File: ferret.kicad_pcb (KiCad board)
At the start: 2 copper layers, 122 parts, among them J201 Power, J301 BAT, J302 BAT, J303 SYS, J401 CHG, J402 CTRL, J403 SOICbite, J404 RS485, Q201 40V, Q202 40V, Q203 40V, SW201 Dead Battery, SW401 RESET, SW402 USER, U201 TPD6S300A, U202 FUSB307BMPX, U203 FSUSB42MUX, U301 TPS560430X3F, U302 BQ25792, U401 STM32F072CBTx, U402 CH340G, U403 SP3485EN, Y401 12MHz

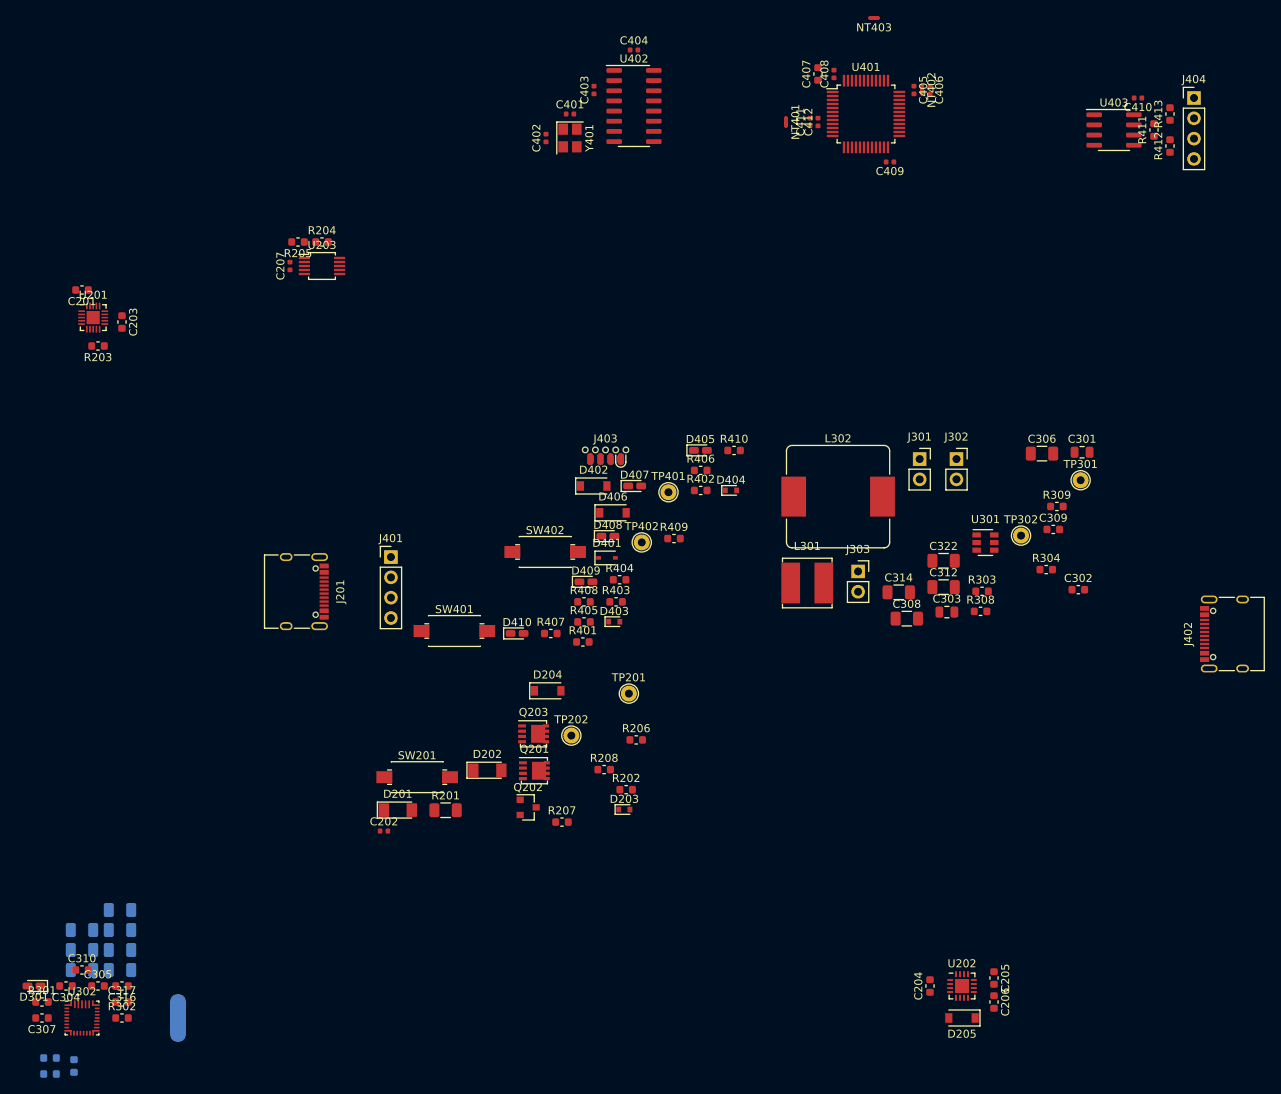
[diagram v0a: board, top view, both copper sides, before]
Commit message: placed to 50x50mm, started to route
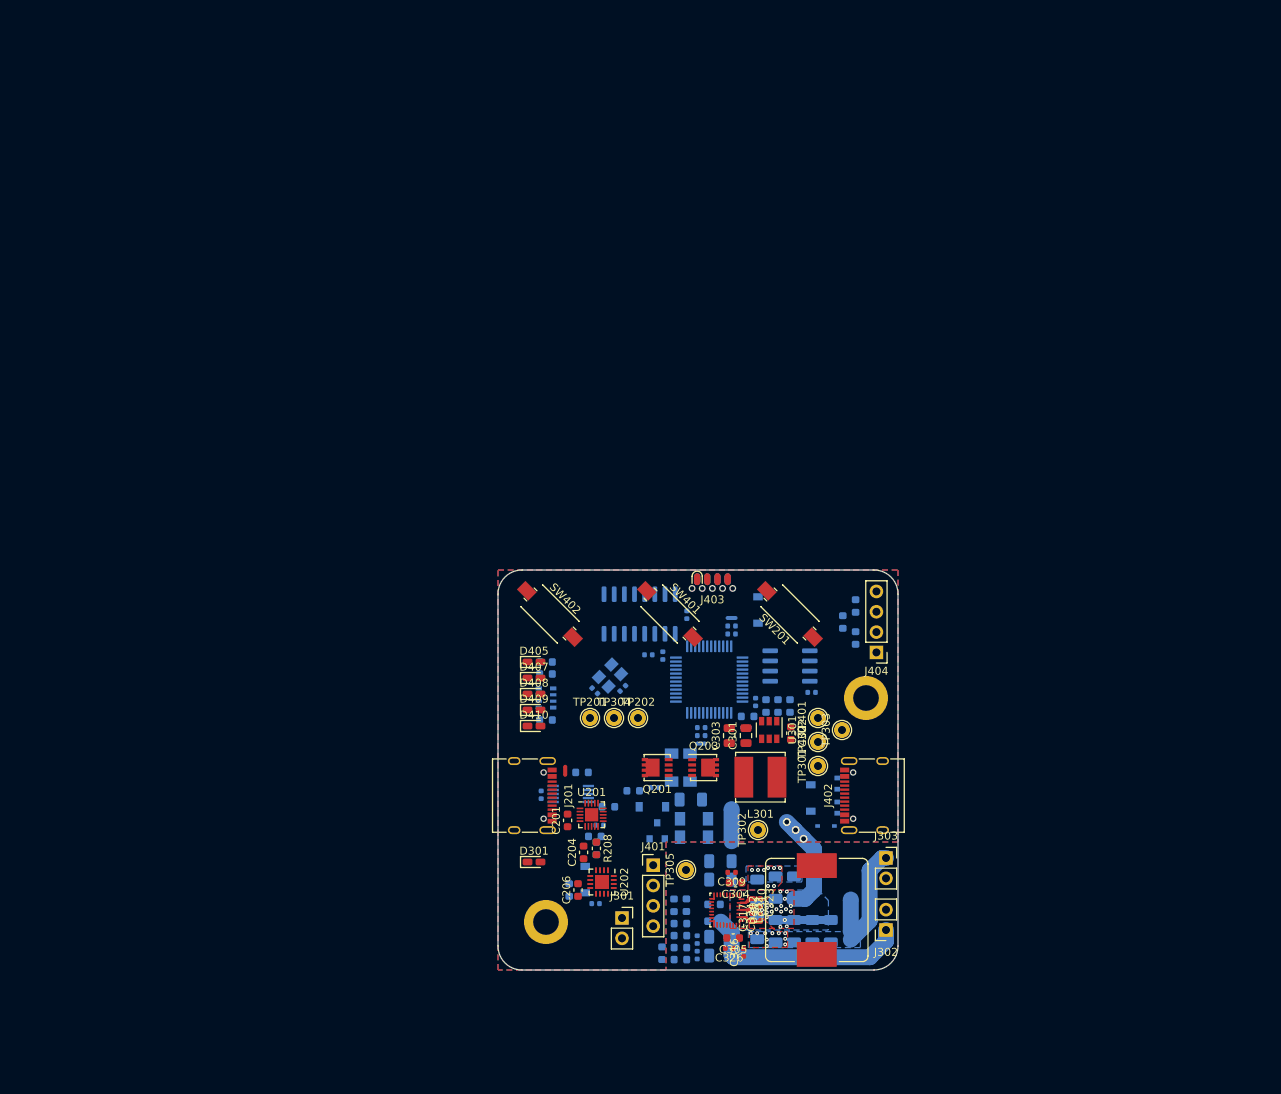
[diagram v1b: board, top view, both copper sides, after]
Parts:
- removed R407, R408, R409: 100, Resistor_SMD:R_0603_1608Metric
- added C323: 100nF, Capacitor_SMD:C_0402_1005Metric, F.Cu at (156.8, 129.6)
- added C324: 100nF, Capacitor_SMD:C_0402_1005Metric, F.Cu at (156.8, 131.4)
- added C326: 100nF, Capacitor_SMD:C_0402_1005Metric, F.Cu at (152.9, 135.3)
- added D206: 3V3, Diode_SMD:D_MiniMELF, B.Cu at (148.0, 112.7)
- added H101: MountingHole_Pad, MountingHole:MountingHole_3.2mm_M3_ISO14580_Pad, F.Cu at (170.0, 104.0)
- added H102: MountingHole_Pad, MountingHole:MountingHole_3.2mm_M3_ISO14580_Pad, F.Cu at (130.0, 132.0)
- added NT1: UwU, NetTie:NetTie-2_SMD_Pad0.5mm, F.Cu at (132.4, 113.1)
- added NT2: chonk_vbus, NetTie:NetTie-2_SMD_Pad2.0mm, B.Cu at (153.2, 119.9)
- added NT302: chonk, NetTie:NetTie-2_SMD_Pad2.0mm, B.Cu at (163.5, 126.0)
- added R310: 470, Resistor_SMD:R_0402_1005Metric, B.Cu at (148.9, 136.1)
- added TP303: GND, TestPoint:TestPoint_THTPad_D2.0mm_Drill1.0mm, F.Cu at (167.0, 108.0)
- added TP304: GND, TestPoint:TestPoint_THTPad_D2.0mm_Drill1.0mm, F.Cu at (138.5, 106.5)
- added TP305: GND1, TestPoint:TestPoint_THTPad_D2.0mm_Drill1.0mm, F.Cu at (147.5, 125.5)
- C202, C203, C205, C207, C306, C307, C308, C312, C314, C322, C401, C402, C403, C404, C405, C406, C407, C408, C409, C410, C411, C412, D201, D202, D204, D205, D401, D402, D403, D404, D406, NT401, NT402, NT403, Q202, R201, R202, R204, R205, R207, R301, R303, R304, R308, R309, R401, R402, R403, R404, R405, R410, R411, R412, R413, U203, U401, U402, U403, Y401: moved to B.Cu
- C309, C310, C316, C317: footprint Capacitor_SMD:C_0603_1608Metric -> Capacitor_SMD:C_0402_1005Metric
- D203: value 12V -> 5V6; footprint Diode_SMD:D_SOD-523 -> Diode_SMD:D_MiniMELF; moved to B.Cu
- R203, R206: footprint Resistor_SMD:R_0603_1608Metric -> Resistor_SMD:R_0402_1005Metric; moved to B.Cu
- R302: value 6.04k -> 5.6k; footprint Resistor_SMD:R_0603_1608Metric -> Resistor_SMD:R_0402_1005Metric; moved to B.Cu
- R406: value 100 -> 470; footprint Resistor_SMD:R_0603_1608Metric -> Resistor_SMD:R_Array_Convex_4x0603; moved to B.Cu
- TP302: value VBUS -> VBUS_BQ
- moved NT403 90.1 mm to (155.0, 107.7)
- moved C201 89.9 mm to (132.7, 119.3), turned to 90 degrees
- moved C311 89.2 mm to (161.0, 127.7), turned to 270 degrees
- moved U201 88.0 mm to (135.7, 118.6)
- moved C203 87.3 mm to (136.1, 121.3), turned to 0 degrees
- moved C313 87.1 mm to (158.7, 127.7), turned to 270 degrees
- moved R203 86.7 mm to (136.7, 119.9)
- moved C318 86.6 mm to (163.3, 133.2), turned to 90 degrees
- moved C307 85.2 mm to (151.0, 129.8)
- moved NT301 85.1 mm to (168.1, 131.2), turned to 270 degrees
- moved C315 85.0 mm to (156.4, 128.1), turned to 270 degrees
- moved C410 84.8 mm to (163.2, 103.3), turned to 0 degrees
- moved C304 84.7 mm to (153.7, 127.1)
- moved C319 84.3 mm to (161.0, 133.2), turned to 90 degrees
- moved C310 84.2 mm to (155.8, 129.6), turned to 270 degrees
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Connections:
- net A renamed /Control/RS485_P
- net B renamed /Control/RS485_N
- net Net-(C302-Pad2) renamed /Power/SW
- net Net-(C304-Pad1) renamed /Power/SW_P
- net Net-(C304-Pad2) renamed /Power/BST1
- net Net-(C305-Pad1) renamed /Power/SW_N
- net Net-(C305-Pad2) renamed /Power/BST2
- net Net-(C310-Pad1) renamed /Power/PMID
- net Net-(C316-Pad2) renamed /Power/SDRV
- net Net-(C401-Pad1) renamed /Control/XT_P
- net Net-(R303-Pad2) renamed /Power/BP
- C306 pad 1: VBUS -> VBUSp
- C306 pad 2: GND -> GND1
- C307 pad 2: GND -> GND1
- C308 pad 1: VBUS -> VBUSp
- C308 pad 2: GND -> GND1
- C309 pad 1: VBUS -> VBUSp
- C309 pad 2: GND -> GND1
- C310 pad 2: GND -> GND1
- C311 pad 2: GND -> GND1
- C312 pad 2: GND -> GND1
- C313 pad 2: GND -> GND1
- C314 pad 2: GND -> GND1
- C315 pad 2: GND -> GND1
- C316 pad 1: GND -> GND1
- C317 pad 2: GND -> GND1
- C318 pad 2: GND -> GND1
- C319 pad 2: GND -> GND1
- C320 pad 2: GND -> GND1
- C321 pad 2: GND -> GND1
- C322 pad 2: GND -> GND1
- C402 pad 1: Net-(C402-Pad1) -> /Control/XT_N
- D203 pad 2: Net-(C202-Pad2) -> Net-(D203-Pad2)
- J201 pad A4: /Input Side/VAC1 -> /Input Side/VBUSRAW
- J201 pad A9: /Input Side/VAC1 -> /Input Side/VBUSRAW
- J201 pad B4: /Input Side/VAC1 -> /Input Side/VBUSRAW
- J201 pad B9: /Input Side/VAC1 -> /Input Side/VBUSRAW
- Q201 pad 2: /Input Side/ACDRV1 -> Net-(C202-Pad2)
- Q201 pad 3: /Input Side/VAC1 -> Net-(C202-Pad2)
- Q201 pad 4: (no net) -> /Input Side/ACDRV1
- Q201 pad 5: (no net) -> /Input Side/VBUSRAW
- Q203 pad 2: /Input Side/ACDRV1 -> Net-(C202-Pad2)
- Q203 pad 3: VBUS -> Net-(C202-Pad2)
- Q203 pad 4: (no net) -> /Input Side/ACDRV1
- Q203 pad 5: (no net) -> VBUS
- R201 pad 1: /Input Side/VAC1 -> /Input Side/VBUSRAW
- R302 pad 2: GND -> Net-(R302-Pad2)
- R306 pad 2: GND -> GND1
- R307 pad 2: GND -> GND1
- R309 pad 2: GND -> GND1
- R406 pad 1: +3V3 -> Net-(D409-Pad2)
- R406 pad 2: Net-(D405-Pad2) -> Net-(D408-Pad2)
- TP302 pad 1: VBUS -> VBUSp
- U302 pad 2: VBUS -> VBUSp
- U302 pad 27: GND -> GND1
- U302 pad 3: VBUS -> VBUSp
- U402 pad 8: Net-(C402-Pad1) -> /Control/XT_N
- Y401 pad 2: Net-(C402-Pad1) -> GND
- Y401 pad 3: (no net) -> /Control/XT_N
- Y401 pad 4: (no net) -> GND
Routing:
- net /Power/VBAT: track 0.00 -> 26.4 mm
- net /Power/SYS: track 0.00 -> 15.1 mm, vias 0 -> 10
- net GND1: track 0.00 -> 11.4 mm, vias 0 -> 21
- net GND: track 0.00 -> 5.91 mm, vias 0 -> 3
- net /Power/PMID: track 0.00 -> 2.70 mm, vias 0 -> 8
- added copper zone on B.Cu, net /Power/PMID
- added copper zone on F.Cu, net /Power/PMID
- added copper zone on B.Cu, net /Power/SYS
- added copper zone on F.Cu, net /Power/SYS
- added copper zone on B.Cu, net GND
- added copper zone on F.Cu, net GND
- added copper zone on B.Cu, net GND1
- added copper zone on F.Cu, net GND1
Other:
- board outline added: 50 x 50 mm
- copper layers 2 -> 4
- net class Default: clearance 0.2 -> 0.15; trace_width 0.25 -> 0.2; via_dia 0.8 -> 0.5; via_drill 0.4 -> 0.2
- net class Thicc added: clearance 0.2, trace_width 2, via_dia 2.4, via_drill 1
- rule pad_to_mask_clearance: 0.05 -> 0.04
- rule trace_clearance: 0.2 -> 0.15
- rule trace_min: 0.2 -> 0.127
- rule via_min_drill: 0.3 -> 0.2
- rule via_min_size: 0.4 -> 0.45

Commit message: partially routed
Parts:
- C310, C317, C323, C324: footprint Capacitor_SMD:C_0402_1005Metric -> Capacitor_SMD:C_0603_1608Metric
- NT301: footprint NetTie:NetTie-2_SMD_Pad2.0mm -> NetTie:NetTie-2_SMD_Pad0.5mm
- R410: value 100 -> 470
- moved NT301 7.42 mm to (169.9, 124.0), turned to 315 degrees
- moved R202 7.38 mm to (148.2, 116.2), turned to 180 degrees
- moved R303 7.14 mm to (145.2, 127.7)
- moved D204 6.90 mm to (148.7, 121.9), turned to 180 degrees
- moved R201 6.61 mm to (143.9, 121.8), turned to 0 degrees
- moved D202 6.59 mm to (143.5, 117.1), turned to 0 degrees
- moved C201 6.41 mm to (139.1, 119.6), turned to 270 degrees
- moved D201 5.01 mm to (143.5, 119.4), turned to 180 degrees
- moved C204 4.88 mm to (132.6, 127.7), turned to 180 degrees
- moved C205 4.54 mm to (137.3, 129.1), turned to 0 degrees
- moved Q202 4.53 mm to (148.1, 118.9), turned to 270 degrees
- moved R207 4.52 mm to (132.6, 125.4)
- moved R208 4.52 mm to (132.6, 125.4)
- moved R206 4.18 mm to (139.0, 126.6), turned to 270 degrees
- moved R203 3.91 mm to (138.3, 116.3)
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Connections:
- net Net-(C202-Pad2) renamed /Input Side/VBS
- D403 pad 1: /Control/D+ -> /Control/SCD+
- D404 pad 1: /Control/D- -> /Control/SCD-
- J402 pad A6: /Control/D+ -> /Control/SCD+
- J402 pad A7: /Control/D- -> /Control/SCD-
- J402 pad B6: /Control/D+ -> /Control/SCD+
- J402 pad B7: /Control/D- -> /Control/SCD-
- U402 pad 5: /Control/D+ -> /Control/SCD+
- U402 pad 6: /Control/D- -> /Control/SCD-
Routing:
- net GND: track 5.91 -> 120.8 mm, vias 3 -> 30
- net +3V3: track 0.00 -> 66.1 mm, vias 0 -> 11
- net /Control/SCD-: track 0.00 -> 55.0 mm, vias 0 -> 3
- net /Control/SCD+: track 0.00 -> 54.3 mm, vias 0 -> 3
- net VCC: track 0.00 -> 34.2 mm, vias 0 -> 1
- net /Input Side/VBUSRAW: track 0.00 -> 33.9 mm, vias 0 -> 11
- net /Control/Blue2: track 0.00 -> 33.5 mm, vias 0 -> 1
- net /Control/Pink2: track 0.00 -> 30.7 mm, vias 0 -> 1
- net /Control/SBU2: track 0.00 -> 28.9 mm
- net /Control/White: track 0.00 -> 28.2 mm, vias 0 -> 1
- net /Control/Pink1: track 0.00 -> 27.2 mm, vias 0 -> 1
- net /Control/Blue1: track 0.00 -> 26.4 mm, vias 0 -> 1
- net /Input Side/CC1: track 0.00 -> 25.2 mm, vias 0 -> 2
- net GND1: track 11.4 -> 35.8 mm, vias 21 -> 28
- net Net-(R401-Pad1): track 0.00 -> 20.5 mm, vias 0 -> 1
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- added copper zone on F.Cu, net /Input Side/VBS
- added copper zone on B.Cu, net /Input Side/VBUSRAW
- added copper zone on F.Cu, net /Input Side/VBUSRAW
- added copper zone on B.Cu, net /Power/VBAT
- added copper zone on F.Cu, net /Power/VBAT
- added copper zone on F.Cu, net VBUS
- added copper zone on B.Cu, net VBUSp
- added copper zone on F.Cu, net VBUSp
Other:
- net class Thicc: clearance 0.2 -> 0.16

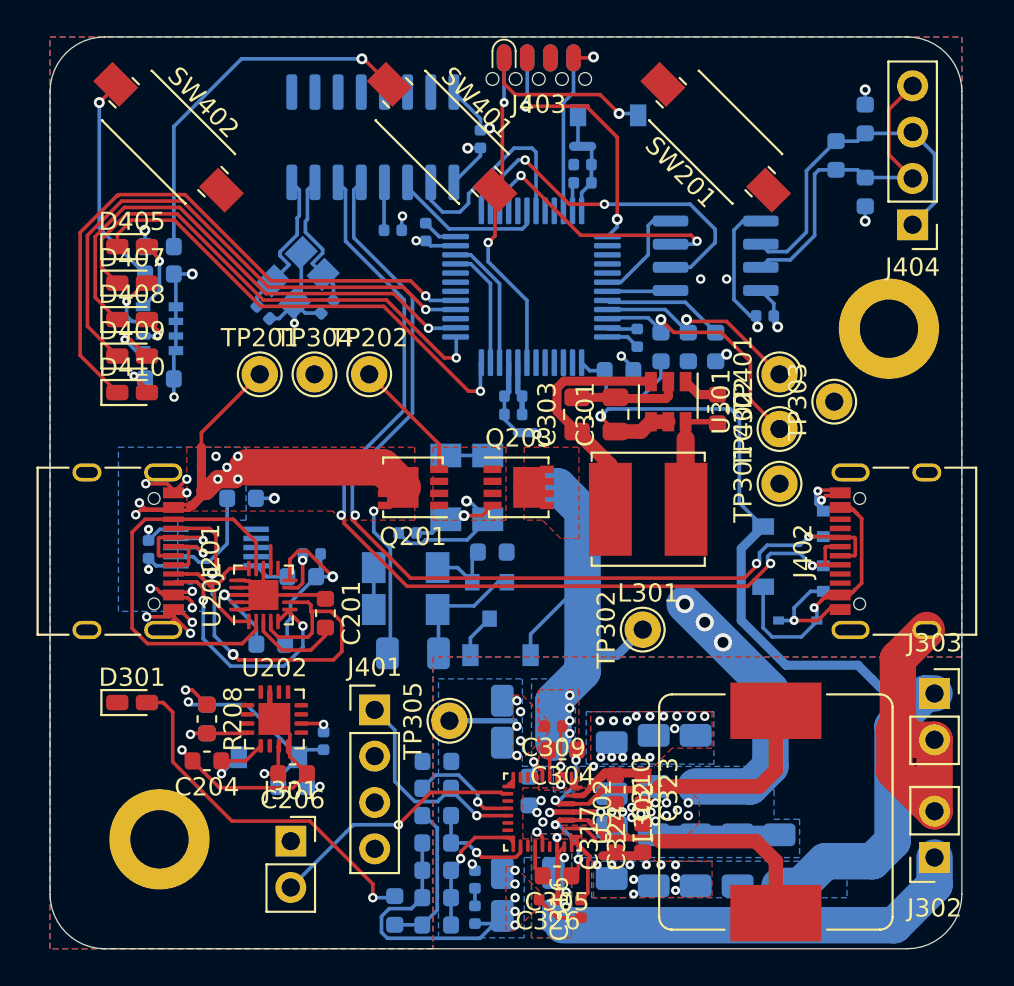
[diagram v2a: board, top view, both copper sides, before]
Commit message: fully routed but silk is still not done
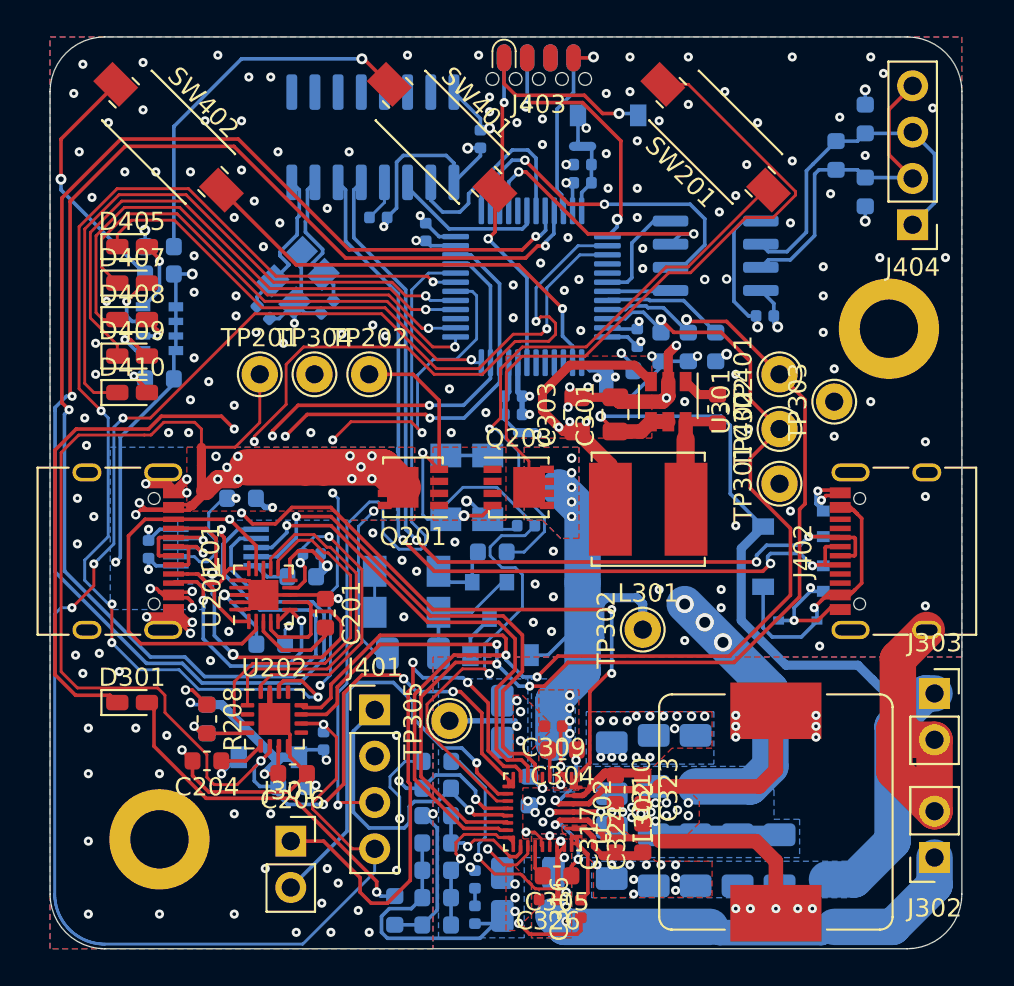
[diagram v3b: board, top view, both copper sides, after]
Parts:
- moved C202 6.51 mm to (150.1, 114.8)
- moved C403 1.06 mm to (142.0, 97.9)
- moved D202 0.21 mm to (143.6, 117.3)
- moved D201 0.16 mm to (143.6, 119.5)
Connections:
- U202 pad 11: /Input Side/SCL -> /Control/SCL
- U202 pad 12: /Input Side/SDA -> /Control/SDA
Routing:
- net /Control/~INT_PMC: track 1.66 -> 95.5 mm, vias 1 -> 5
- net /Control/D+: track 0.00 -> 82.4 mm, vias 0 -> 2
- net /Control/D-: track 0.00 -> 81.2 mm, vias 0 -> 2
- net /Input Side/EN_SINK: track 0.00 -> 68.5 mm, vias 0 -> 5
- net Net-(D301-Pad1): track 0.66 -> 68.3 mm, vias 0 -> 4
- net /Input Side/VAC1: track 5.78 -> 70.7 mm, vias 0 -> 4
- net /Control/SCL: track 12.1 -> 73.3 mm, vias 1 -> 4
- net /Control/SDA: track 14.3 -> 74.5 mm, vias 1 -> 3
- net /Control/~INT_CHG: track 0.00 -> 52.9 mm, vias 0 -> 2
- net /Control/~CE: track 12.0 -> 51.2 mm, vias 1 -> 5
- net /Input Side/ACDRV1: track 11.6 -> 48.0 mm, vias 1 -> 3
- net VBUS: track 12.4 -> 48.1 mm, vias 0 -> 5
- net /Control/USB_SEL: track 5.84 -> 40.6 mm, vias 0 -> 3
- net Net-(R202-Pad1): track 0.00 -> 31.9 mm, vias 0 -> 1
- net /Power/VAC2: track 0.00 -> 31.5 mm, vias 0 -> 2
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- added copper zone on F.Cu, net +3V3
- added copper zone on In1.Cu, net +3V3
- added copper zone on In1.Cu, net /Control/VDD
- added copper zone on In1.Cu, net /Power/SW_N
- added copper zone on In1.Cu, net /Power/SW_P
- added copper zone on In1.Cu, net GND
- added copper zone on In2.Cu, net GND
- added copper zone on B.Cu, net VBUS
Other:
- rule pad_to_mask_clearance: 0.04 -> 0
